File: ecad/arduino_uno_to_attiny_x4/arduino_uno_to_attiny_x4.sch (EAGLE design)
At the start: 3 parts

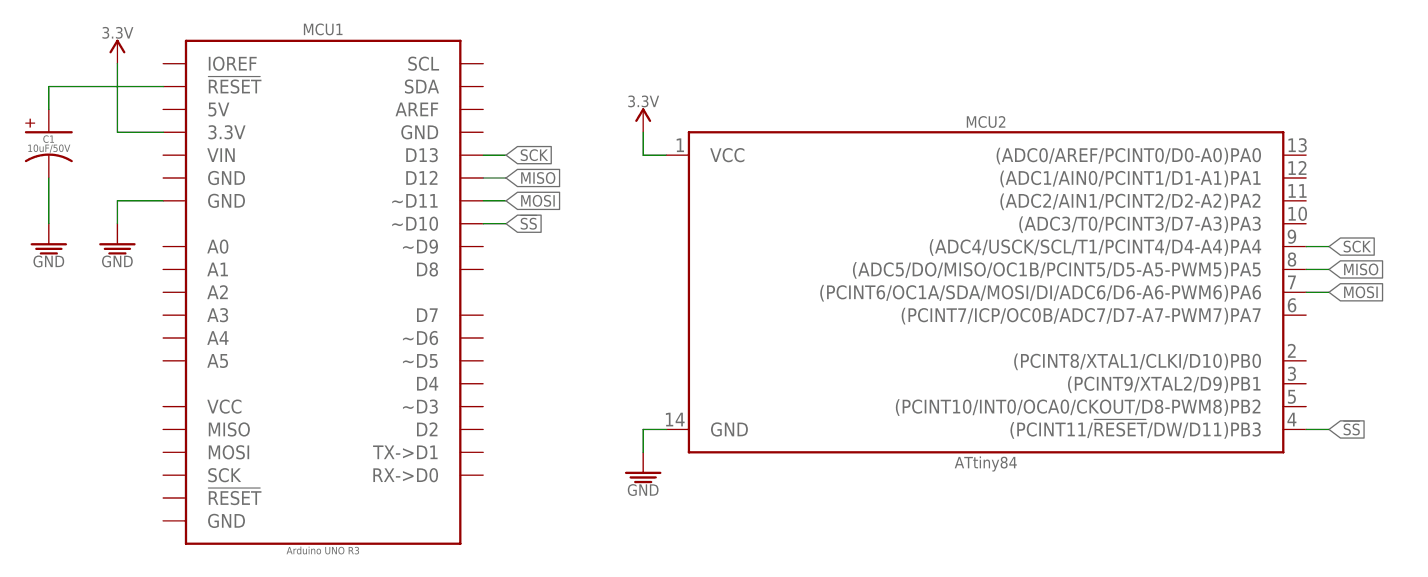
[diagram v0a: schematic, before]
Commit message: Update ATtiny84 symbol to match the CCW ATtiny core.
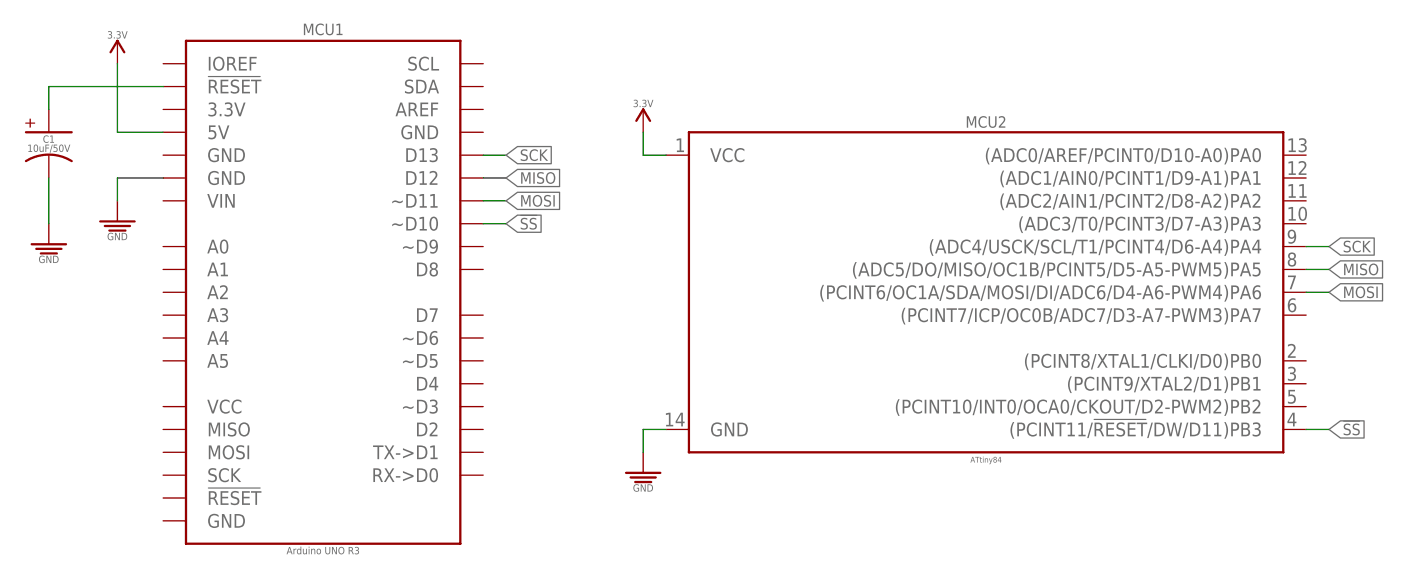
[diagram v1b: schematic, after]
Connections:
- net 3.3V: now also MCU1.5V; no longer MCU1.3.3V
- net MOSI: now also MCU2.(PCINT6/OC1A/SDA/MOSI/DI/ADC6/D4-A6-PWM4)PA6; no longer MCU2.(PCINT6/OC1A/SDA/MOSI/DI/ADC6/D6-A6-PWM6)PA6
- net SCK: now also MCU2.(ADC4/USCK/SCL/T1/PCINT4/D6-A4)PA4; no longer MCU2.(ADC4/USCK/SCL/T1/PCINT4/D4-A4)PA4
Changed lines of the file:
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@@
 <?xml version="1.0" encoding="utf-8"?>
 <!DOCTYPE eagle SYSTEM "eagle.dtd">
-<eagle version="9.1.1">
+<eagle version="9.2.2">
 <drawing>
 <settings>
@@
 </plain>
 <instances>
-<instance part="MCU1" gate="G$1" x="38.1" y="35.56"/>
-<instance part="SUPPLY1" gate="GND" x="73.66" y="15.24"/>
-<instance part="SUPPLY2" gate="GND" x="15.24" y="40.64"/>
-<instance part="SUPPLY3" gate="3.3V" x="15.24" y="60.96"/>
-<instance part="SUPPLY4" gate="3.3V" x="73.66" y="53.34"/>
-<instance part="C1" gate="G$1" x="7.62" y="53.34"/>
-<instance part="SUPPLY5" gate="GND" x="7.62" y="40.64"/>
-<instance part="MCU2" gate="G$1" x="111.76" y="35.56"/>
+<instance part="MCU1" gate="G$1" x="38.1" y="35.56" smashed="yes">
+<attribute name="NAME" x="38.1" y="64.77" size="1.27" layer="95" font="vector" ratio="10" align="center"/>
+<attribute name="VALUE" x="38.1" y="6.858" size="0.8128" layer="96" font="vector" ratio="10" align="center"/>
+</instance>
+<instance part="SUPPLY1" gate="GND" x="73.66" y="15.24" smashed="yes"/>
+<instance part="SUPPLY2" gate="GND" x="15.24" y="43.18" smashed="yes"/>
+<instance part="SUPPLY3" gate="3.3V" x="15.24" y="60.96" smashed="yes"/>
+<instance part="SUPPLY4" gate="3.3V" x="73.66" y="53.34" smashed="yes"/>
+<instance part="C1" gate="G$1" x="7.62" y="53.34" smashed="yes">
+<attribute name="NAME" x="7.62" y="52.578" size="0.8128" layer="95" font="vector" ratio="10" align="center"/>
+<attribute name="VALUE" x="7.62" y="51.562" size="0.8128" layer="96" font="vector" ratio="10" align="center"/>
+</instance>
+<instance part="SUPPLY5" gate="GND" x="7.62" y="40.64" smashed="yes"/>
+<instance part="MCU2" gate="G$1" x="111.76" y="35.56" smashed="yes">
+<attribute name="VALUE" x="111.76" y="17.272" size="0.635" layer="96" font="vector" ratio="10" align="top-center"/>
+<attribute name="NAME" x="111.76" y="53.848" size="1.27" layer="95" font="vector" ratio="10" align="bottom-center"/>
+</instance>
 </instances>
 <busses>
@@
 <segment>
 <pinref part="SUPPLY2" gate="GND" pin="GND"/>
-<wire x1="15.24" y1="43.18" x2="15.24" y2="45.72" width="0.1524" layer="91"/>
+<wire x1="15.24" y1="45.72" x2="15.24" y2="48.26" width="0.1524" layer="91"/>
 <pinref part="MCU1" gate="G$1" pin="GND@1"/>
-<wire x1="15.24" y1="45.72" x2="20.32" y2="45.72" width="0.1524" layer="91"/>
+<wire x1="15.24" y1="48.26" x2="20.32" y2="48.26" width="0.1524" layer="91"/>
 </segment>
 <segment>
@@
 <net name="3.3V" class="0">
 <segment>
-<pinref part="MCU1" gate="G$1" pin="3.3V"/>
+<pinref part="MCU1" gate="G$1" pin="5V"/>
 <wire x1="20.32" y1="53.34" x2="15.24" y2="53.34" width="0.1524" layer="91"/>
 <wire x1="15.24" y1="53.34" x2="15.24" y2="60.96" width="0.1524" layer="91"/>
@@
 <wire x1="149.86" y1="35.56" x2="147.32" y2="35.56" width="0.1524" layer="91"/>
 <label x="149.86" y="35.56" size="1.27" layer="95" font="vector" ratio="10" xref="yes"/>
-<pinref part="MCU2" gate="G$1" pin="(PCINT6/OC1A/SDA/MOSI/DI/ADC6/D6-A6-PWM6)PA6"/>
+<pinref part="MCU2" gate="G$1" pin="(PCINT6/OC1A/SDA/MOSI/DI/ADC6/D4-A6-PWM4)PA6"/>
 </segment>
 <segment>
@@
 <wire x1="147.32" y1="40.64" x2="149.86" y2="40.64" width="0.1524" layer="91"/>
 <label x="149.86" y="40.64" size="1.27" layer="95" font="vector" ratio="10" xref="yes"/>
-<pinref part="MCU2" gate="G$1" pin="(ADC4/USCK/SCL/T1/PCINT4/D4-A4)PA4"/>
-</segment>
-<segment>
+<pinref part="MCU2" gate="G$1" pin="(ADC4/USCK/SCL/T1/PCINT4/D6-A4)PA4"/>
+</segment>
+<segment>

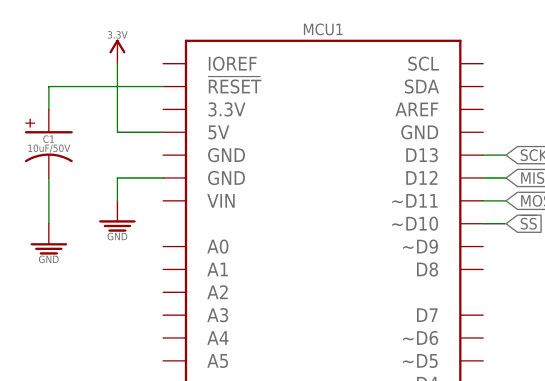
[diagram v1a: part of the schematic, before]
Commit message: Fix mistake connecting to 5V
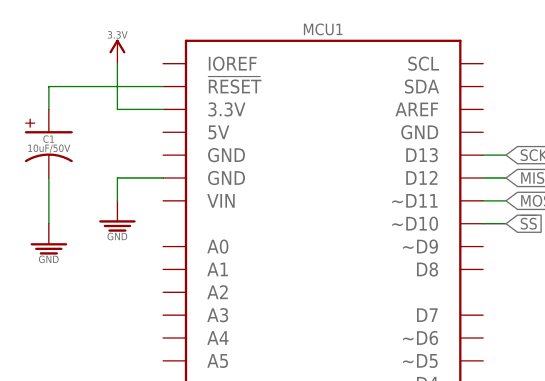
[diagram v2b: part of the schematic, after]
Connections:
- net 3.3V: now also MCU1.3.3V; no longer MCU1.5V
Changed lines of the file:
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@@
 <net name="3.3V" class="0">
-<segment>
-<pinref part="MCU1" gate="G$1" pin="5V"/>
-<wire x1="20.32" y1="53.34" x2="15.24" y2="53.34" width="0.1524" layer="91"/>
-<wire x1="15.24" y1="53.34" x2="15.24" y2="60.96" width="0.1524" layer="91"/>
-<pinref part="SUPPLY3" gate="3.3V" pin="3.3V"/>
-</segment>
 <segment>
 <wire x1="76.2" y1="50.8" x2="73.66" y2="50.8" width="0.1524" layer="91"/>
@@
 <pinref part="MCU2" gate="G$1" pin="VCC"/>
 </segment>
+<segment>
+<pinref part="SUPPLY3" gate="3.3V" pin="3.3V"/>
+<pinref part="MCU1" gate="G$1" pin="3.3V"/>
+<wire x1="15.24" y1="60.96" x2="15.24" y2="55.88" width="0.1524" layer="91"/>
+<wire x1="15.24" y1="55.88" x2="20.32" y2="55.88" width="0.1524" layer="91"/>
+</segment>
 </net>
